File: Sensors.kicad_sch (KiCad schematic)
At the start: 13 parts, among them U5 BME280, U6 MPU-6050

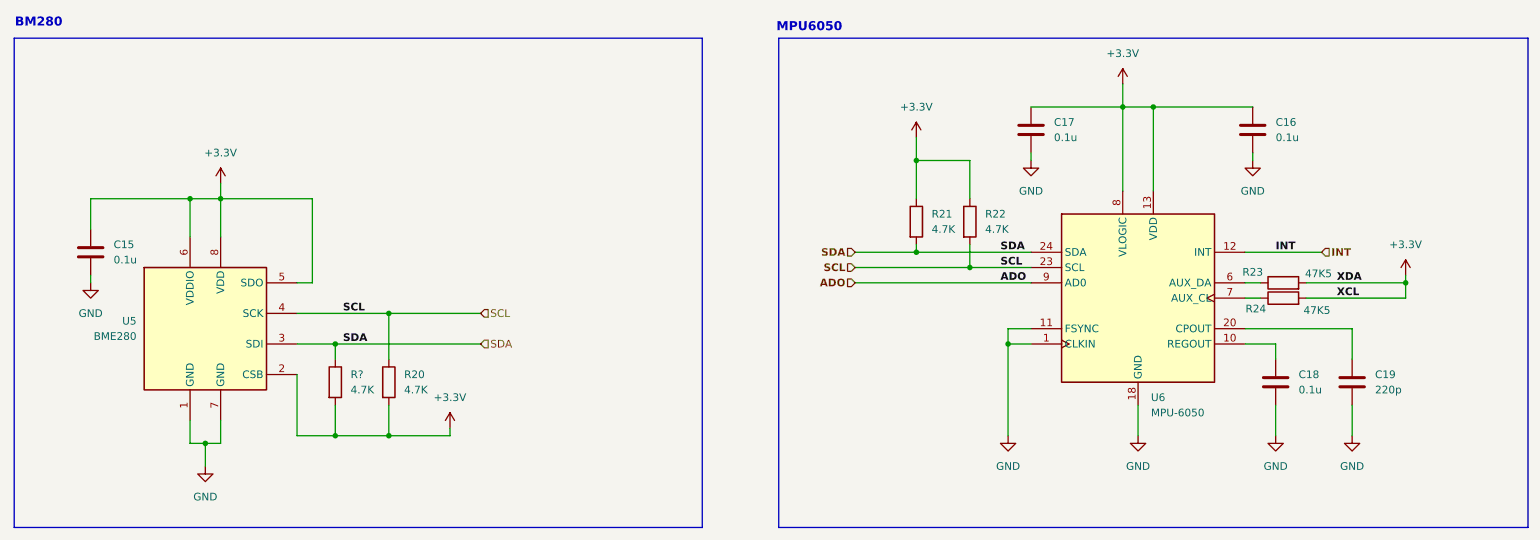
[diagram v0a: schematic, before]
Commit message: fix(sch): reroute sensor wiring and update component references
Adjusted wire connections and component labels in the sensors schematic to correct routing paths and ensure proper connectivity. Updated power reference identifiers to maintain consistency with the revised component layout.
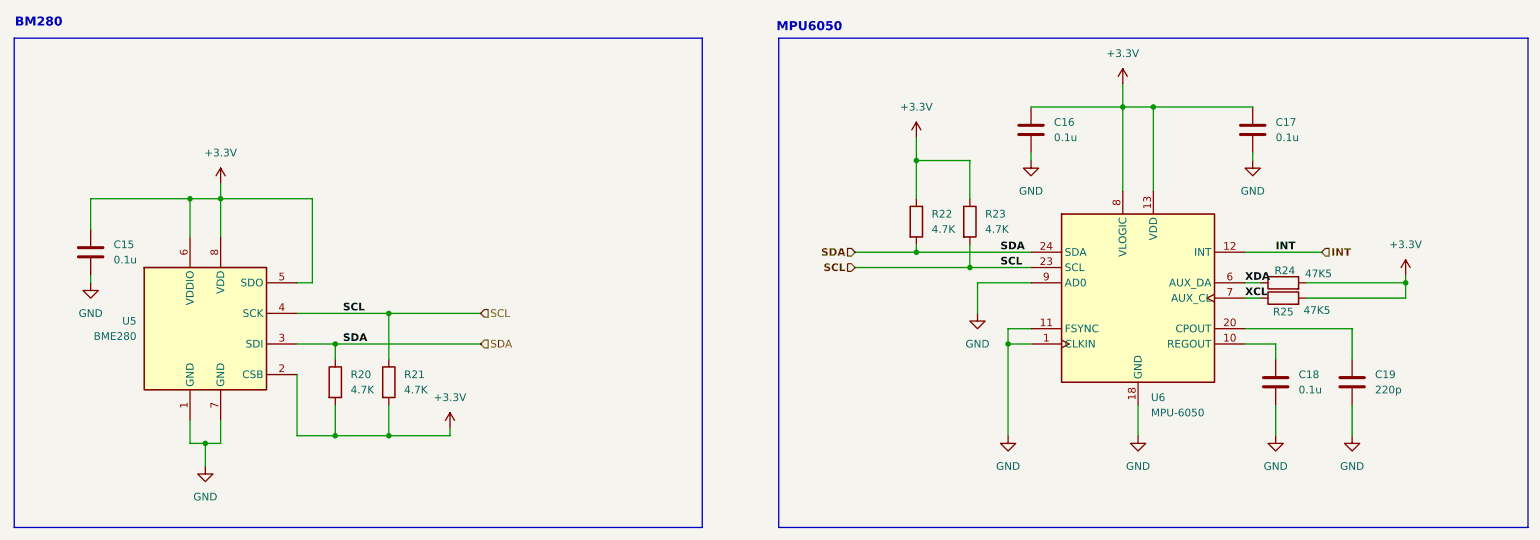
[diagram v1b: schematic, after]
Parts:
- removed R?: 4.7K, Resistor_SMD:R_0201_0603Metric, symbol Device:R
- added R20: 4.7K, Resistor_SMD:R_0201_0603Metric, symbol Device:R
- renumbered C17 to C16, C16 to C17, R20 to R21, R21 to R22, R22 to R23, R23 to R24, R24 to R25
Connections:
- net ADO is gone; now on net GND: U6.9 (AD0)
- net +3.3V: now also R20.2
- net SDA: now also R20.1
- net XDA: now reaches R24.1, U6.6 (AUX_DA)
- net XCL: now reaches R25.1, U6.7 (AUX_CL)

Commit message: fix(sch): update component and power reference designators
Update various component references (C14, C15, C16) and power net labels
(#PWR050, #PWR051, #PWR053, #PWR055, #PWR056) in the Sensors schematic
to ensure correct netlist consistency.
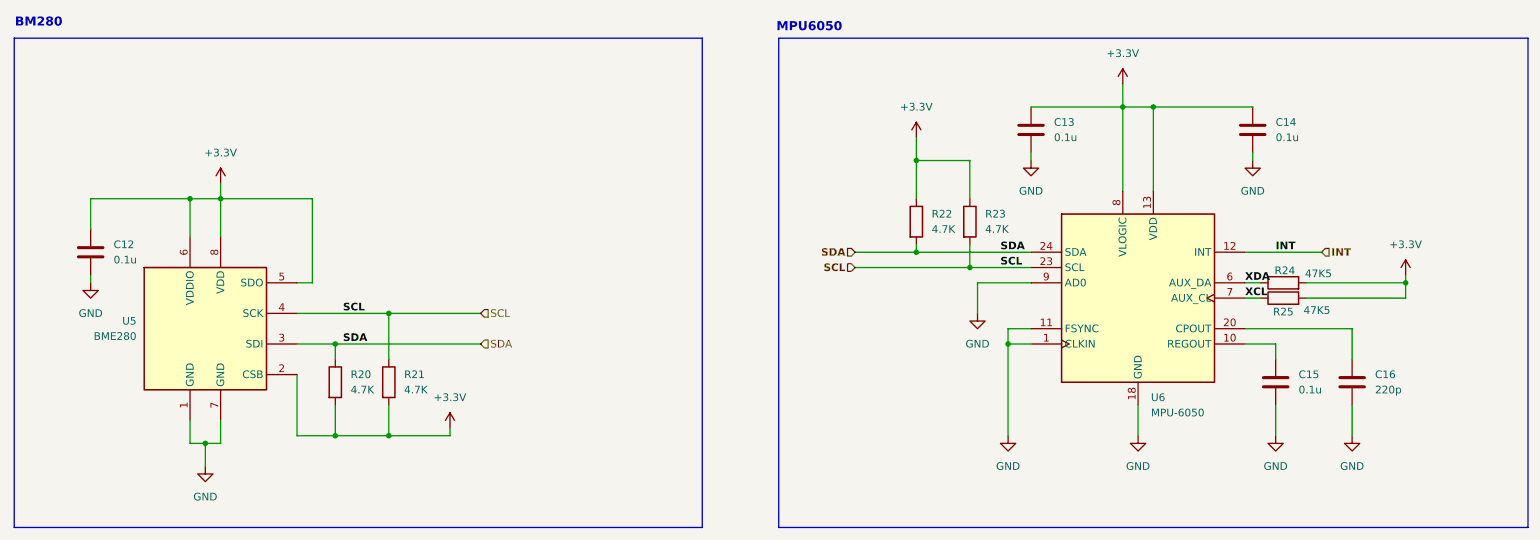
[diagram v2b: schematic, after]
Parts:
- renumbered C15 to C12, C16 to C13, C17 to C14, C18 to C15, C19 to C16
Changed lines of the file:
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@@
 		(dnp no)
 		(fields_autoplaced yes)
-		(property "Reference" "#PWR049"
+		(property "Reference" "#PWR050"
 			(at 196.85 77.47 0)
 			(effects
@@
 			(project "iot_device_pcb"
 				(path "/20a6db8f-6f9d-426b-a90e-3cd30ac36ee8/d76e5a61-e019-4441-8e0f-87cbb4ce42a5/bd1ed058-0d95-47ef-a7d2-a0812ed5db5b"
-					(reference "#PWR049")
+					(reference "#PWR050")
 					(unit 1)
 				)
@@
 		(dnp no)
 		(fields_autoplaced yes)
-		(property "Reference" "C19"
+		(property "Reference" "C16"
 			(at 254 106.6799 0)
 			(effects
@@
 			(project "iot_device_pcb"
 				(path "/20a6db8f-6f9d-426b-a90e-3cd30ac36ee8/d76e5a61-e019-4441-8e0f-87cbb4ce42a5/bd1ed058-0d95-47ef-a7d2-a0812ed5db5b"
-					(reference "C19")
+					(reference "C16")
 					(unit 1)
 				)
@@
 		(dnp no)
 		(fields_autoplaced yes)
-		(property "Reference" "#PWR050"
+		(property "Reference" "#PWR051"
 			(at 212.09 62.23 0)
 			(effects
@@
 			(project "iot_device_pcb"
 				(path "/20a6db8f-6f9d-426b-a90e-3cd30ac36ee8/d76e5a61-e019-4441-8e0f-87cbb4ce42a5/bd1ed058-0d95-47ef-a7d2-a0812ed5db5b"
-					(reference "#PWR050")
+					(reference "#PWR051")
 					(unit 1)
 				)
@@
 		(dnp no)
 		(fields_autoplaced yes)
-		(property "Reference" "C18"
+		(property "Reference" "C15"
 			(at 241.3 106.6799 0)
 			(effects
@@
 			(project "iot_device_pcb"
 				(path "/20a6db8f-6f9d-426b-a90e-3cd30ac36ee8/d76e5a61-e019-4441-8e0f-87cbb4ce42a5/bd1ed058-0d95-47ef-a7d2-a0812ed5db5b"
-					(reference "C18")
+					(reference "C15")
 					(unit 1)
 				)
@@
 		(on_board yes)
 		(dnp no)
-		(property "Reference" "#PWR054"
+		(property "Reference" "#PWR055"
 			(at 250.19 123.19 0)
 			(effects
@@
 			(project "iot_device_pcb"
 				(path "/20a6db8f-6f9d-426b-a90e-3cd30ac36ee8/d76e5a61-e019-4441-8e0f-87cbb4ce42a5/bd1ed058-0d95-47ef-a7d2-a0812ed5db5b"
-					(reference "#PWR054")
+					(reference "#PWR055")
 					(unit 1)
 				)
@@
 		(dnp no)
 		(fields_autoplaced yes)
-		(property "Reference" "C17"
+		(property "Reference" "C14"
 			(at 237.49 64.7699 0)
 			(effects
@@
 			(project "iot_device_pcb"
 				(path "/20a6db8f-6f9d-426b-a90e-3cd30ac36ee8/d76e5a61-e019-4441-8e0f-87cbb4ce42a5/bd1ed058-0d95-47ef-a7d2-a0812ed5db5b"
-					(reference "C17")
+					(reference "C14")
 					(unit 1)
 				)
@@
 		(dnp no)
 		(fields_autoplaced yes)
-		(property "Reference" "#PWR055"
+		(property "Reference" "#PWR056"
 			(at 259.08 93.98 0)
 			(effects
@@
 			(project "iot_device_pcb"
 				(path "/20a6db8f-6f9d-426b-a90e-3cd30ac36ee8/d76e5a61-e019-4441-8e0f-87cbb4ce42a5/bd1ed058-0d95-47ef-a7d2-a0812ed5db5b"
-					(reference "#PWR055")
+					(reference "#PWR056")
 					(unit 1)
 				)
@@
 		(dnp no)
 		(fields_autoplaced yes)
-		(property "Reference" "#PWR052"
+		(property "Reference" "#PWR053"
 			(at 233.68 77.47 0)
 			(effects
@@
 			(project "iot_device_pcb"
 				(path "/20a6db8f-6f9d-426b-a90e-3cd30ac36ee8/d76e5a61-e019-4441-8e0f-87cbb4ce42a5/bd1ed058-0d95-47ef-a7d2-a0812ed5db5b"
-					(reference "#PWR052")
+					(reference "#PWR053")
 					(unit 1)
 				)
@@
 		(dnp no)
 		(fields_autoplaced yes)
-		(property "Reference" "C16"
+		(property "Reference" "C13"
 			(at 200.66 64.7699 0)
 			(effects
@@
 			(project "iot_device_pcb"
 				(path "/20a6db8f-6f9d-426b-a90e-3cd30ac36ee8/d76e5a61-e019-4441-8e0f-87cbb4ce42a5/bd1ed058-0d95-47ef-a7d2-a0812ed5db5b"
-					(reference "C16")
+					(reference "C13")
 					(unit 1)
 				)
@@
 		(dnp no)
 		(fields_autoplaced yes)
-		(property "Reference" "C15"
+		(property "Reference" "C12"
 			(at 44.45 85.0899 0)
 			(effects
@@
 			(project "iot_device_pcb"
 				(path "/20a6db8f-6f9d-426b-a90e-3cd30ac36ee8/d76e5a61-e019-4441-8e0f-87cbb4ce42a5/bd1ed058-0d95-47ef-a7d2-a0812ed5db5b"
-					(reference "C15")
+					(reference "C12")
 					(unit 1)
 				)
@@
 		(on_board yes)
 		(dnp no)
-		(property "Reference" "#PWR053"
+		(property "Reference" "#PWR054"
 			(at 237.49 123.19 0)
 			(effects
@@
 			(project "iot_device_pcb"
 				(path "/20a6db8f-6f9d-426b-a90e-3cd30ac36ee8/d76e5a61-e019-4441-8e0f-87cbb4ce42a5/bd1ed058-0d95-47ef-a7d2-a0812ed5db5b"
-					(reference "#PWR053")
+					(reference "#PWR054")
 					(unit 1)
 				)
@@
 		(dnp no)
 		(fields_autoplaced yes)
-		(property "Reference" "#PWR048"
+		(property "Reference" "#PWR049"
 			(at 193.04 123.19 0)
 			(effects
@@
 			(project "iot_device_pcb"
 				(path "/20a6db8f-6f9d-426b-a90e-3cd30ac36ee8/d76e5a61-e019-4441-8e0f-87cbb4ce42a5/bd1ed058-0d95-47ef-a7d2-a0812ed5db5b"
-					(reference "#PWR048")
+					(reference "#PWR049")
 					(unit 1)
 				)
@@
 		(dnp no)
 		(fields_autoplaced yes)
-		(property "Reference" "#PWR062"
+		(property "Reference" "#PWR048"
 			(at 187.96 102.87 0)
 			(effects
@@
 			(project ""
 				(path "/20a6db8f-6f9d-426b-a90e-3cd30ac36ee8/d76e5a61-e019-4441-8e0f-87cbb4ce42a5/bd1ed058-0d95-47ef-a7d2-a0812ed5db5b"
-					(reference "#PWR062")
+					(reference "#PWR048")
 					(unit 1)
 				)
@@
 		(dnp no)
 		(fields_autoplaced yes)
-		(property "Reference" "#PWR051"
+		(property "Reference" "#PWR052"
 			(at 214.63 123.19 0)
 			(effects
@@
 			(project ""
 				(path "/20a6db8f-6f9d-426b-a90e-3cd30ac36ee8/d76e5a61-e019-4441-8e0f-87cbb4ce42a5/bd1ed058-0d95-47ef-a7d2-a0812ed5db5b"
-					(reference "#PWR051")
-					(unit 1)
-				)
+					(reference "#PWR052")
+					(unit 1)
+				)
